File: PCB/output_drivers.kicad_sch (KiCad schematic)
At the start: 5 parts, among them U2 TL072, U3 TL072

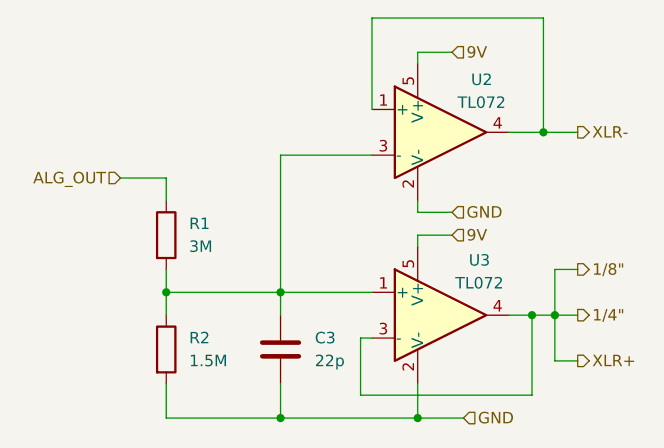
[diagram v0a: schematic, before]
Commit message: reorganized MATLAB and PCB files, merged analog design into main KiCAD schematic, added MATLAB noise analysis
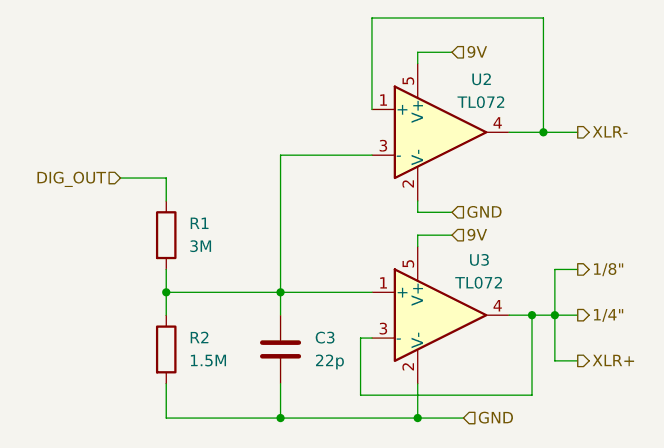
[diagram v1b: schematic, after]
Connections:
- net ALG_OUT renamed DIG_OUT
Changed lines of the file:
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@@
 		)
 	)
-	(hierarchical_label "ALG_OUT"
+	(hierarchical_label "DIG_OUT"
 		(shape input)
 		(at 104.14 92.71 180)
